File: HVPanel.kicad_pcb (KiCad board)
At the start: 2 copper layers, 7 parts, among them U1 VICOR

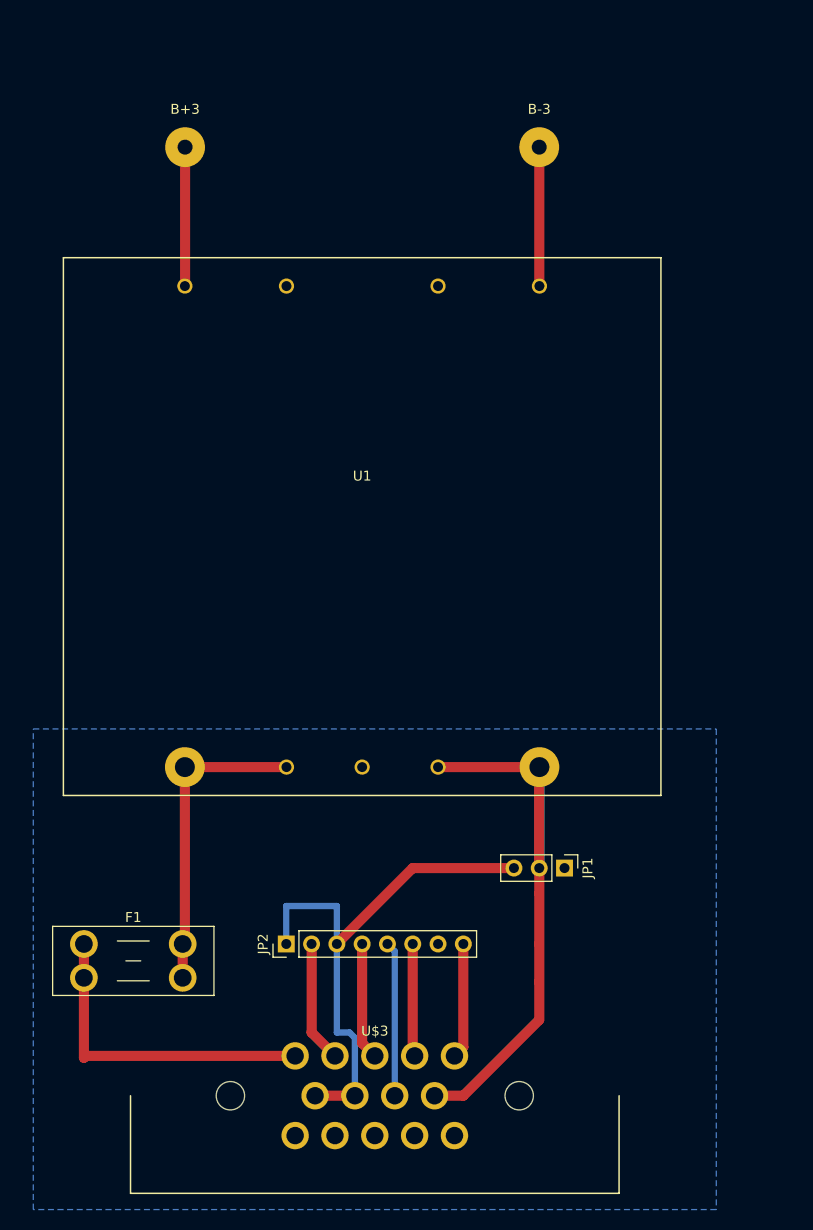
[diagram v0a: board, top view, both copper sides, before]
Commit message: Added dimensions
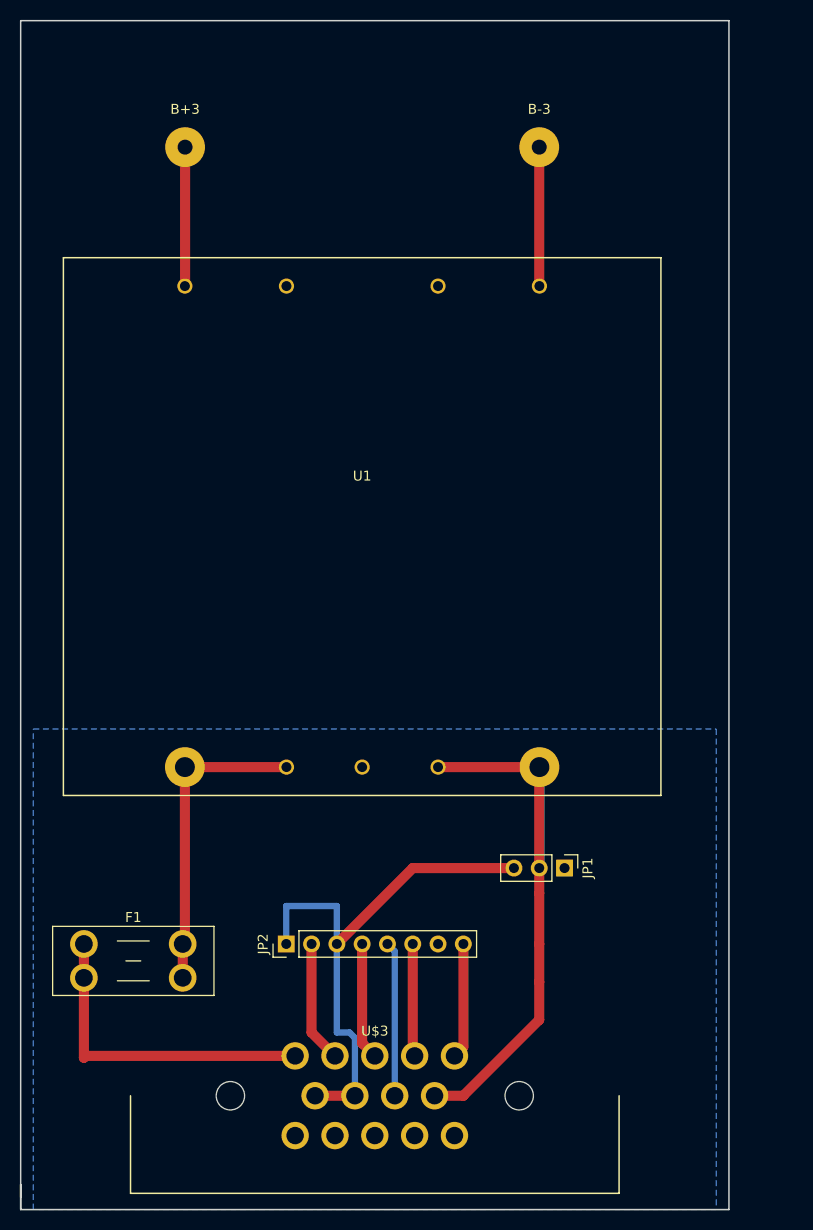
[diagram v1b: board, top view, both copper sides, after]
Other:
- board outline added: 71.1 x 119.4 mm

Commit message: added hole
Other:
- board size 71.1 x 119.4 mm -> 77.5 x 119.4 mm
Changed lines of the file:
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@@
     (links 19)
     (no_connects 0)
-    (area 67.31 46.015 135.890001 157.480001)
+    (area 57.555716 38.024999 158.344286 167.640001)
     (thickness 1.6)
-    (drawings 16)
+    (drawings 25)
     (tracks 42)
     (zones 0)
@@
     (pad "" np_thru_hole circle (at 14.5 0) (size 2.85 2.85) (drill 2.85) (layers *.Cu *.Mask))
   )
+  (dimension 3.592102 (width 0.3) (layer F.Fab)
+    (gr_text "3.592 mm" (at 141.289594 75.880405 315) (layer F.Fab)
+      (effects (font (size 1.5 1.5) (thickness 0.3)))
+    )
+    (feature1 (pts (xy 135.89 83.82) (xy 143.514189 76.195811)))
+    (feature2 (pts (xy 133.35 81.28) (xy 140.974189 73.655811)))
+    (crossbar (pts (xy 139.065 75.565) (xy 141.605 78.105)))
+    (arrow1a (pts (xy 141.605 78.105) (xy 140.393779 77.723104)))
+    (arrow1b (pts (xy 141.605 78.105) (xy 141.223104 76.893779)))
+    (arrow2a (pts (xy 139.065 75.565) (xy 139.446896 76.776221)))
+    (arrow2b (pts (xy 139.065 75.565) (xy 140.276221 75.946896)))
+  )
+  (gr_circle (center 134.62 82.55) (end 135.89 83.82) (layer Edge.Cuts) (width 0.15))
+  (dimension 3.81 (width 0.3) (layer F.Fab)
+    (gr_text "3.810 mm" (at 133.985 95.33) (layer F.Fab)
+      (effects (font (size 1.5 1.5) (thickness 0.3)))
+    )
+    (feature1 (pts (xy 135.89 81.28) (xy 135.89 96.68)))
+    (feature2 (pts (xy 132.08 81.28) (xy 132.08 96.68)))
+    (crossbar (pts (xy 132.08 93.98) (xy 135.89 93.98)))
+    (arrow1a (pts (xy 135.89 93.98) (xy 134.763496 94.566421)))
+    (arrow1b (pts (xy 135.89 93.98) (xy 134.763496 93.393579)))
+    (arrow2a (pts (xy 132.08 93.98) (xy 133.206504 94.566421)))
+    (arrow2b (pts (xy 132.08 93.98) (xy 133.206504 93.393579)))
+  )
+  (dimension 10.16 (width 0.3) (layer F.Fab)
+    (gr_text "10.160 mm" (at 138.43 86.36) (layer F.Fab)
+      (effects (font (size 1.5 1.5) (thickness 0.3)))
+    )
+    (feature1 (pts (xy 133.35 83.82) (xy 133.35 83.82)))
+    (feature2 (pts (xy 143.51 83.82) (xy 143.51 83.82)))
+    (crossbar (pts (xy 143.51 83.82) (xy 133.35 83.82)))
+    (arrow1a (pts (xy 133.35 83.82) (xy 134.476504 83.233579)))
+    (arrow1b (pts (xy 133.35 83.82) (xy 134.476504 84.406421)))
+    (arrow2a (pts (xy 143.51 83.82) (xy 142.383496 83.233579)))
+    (arrow2b (pts (xy 143.51 83.82) (xy 142.383496 84.406421)))
+  )
+  (dimension 8.89 (width 0.3) (layer F.Fab)
+    (gr_text "8.890 mm" (at 140.97 80.01) (layer F.Fab)
+      (effects (font (size 1.5 1.5) (thickness 0.3)))
+    )
+    (feature1 (pts (xy 134.62 81.28) (xy 134.62 83.98)))
+    (feature2 (pts (xy 143.51 81.28) (xy 143.51 83.98)))
+    (crossbar (pts (xy 143.51 81.28) (xy 134.62 81.28)))
+    (arrow1a (pts (xy 134.62 81.28) (xy 135.746504 80.693579)))
+    (arrow1b (pts (xy 134.62 81.28) (xy 135.746504 81.866421)))
+    (arrow2a (pts (xy 143.51 81.28) (xy 142.383496 80.693579)))
+    (arrow2b (pts (xy 143.51 81.28) (xy 142.383496 81.866421)))
+  )
+  (gr_line (start 137.16 38.1) (end 143.51 38.1) (angle 90) (layer Edge.Cuts) (width 0.15))
+  (gr_line (start 140.97 157.48) (end 143.51 157.48) (angle 90) (layer F.Fab) (width 0.2))
+  (dimension 74.93 (width 0.3) (layer F.Fab)
+    (gr_text "74.930 mm" (at 103.505 162.64) (layer F.Fab)
+      (effects (font (size 1.5 1.5) (thickness 0.3)))
+    )
+    (feature1 (pts (xy 140.97 161.29) (xy 140.97 163.99)))
+    (feature2 (pts (xy 66.04 161.29) (xy 66.04 163.99)))
+    (crossbar (pts (xy 66.04 161.29) (xy 140.97 161.29)))
+    (arrow1a (pts (xy 140.97 161.29) (xy 139.843496 161.876421)))
+    (arrow1b (pts (xy 140.97 161.29) (xy 139.843496 160.703579)))
+    (arrow2a (pts (xy 66.04 161.29) (xy 67.166504 161.876421)))
+    (arrow2b (pts (xy 66.04 161.29) (xy 67.166504 160.703579)))
+  )
+  (dimension 68.58 (width 0.3) (layer F.Fab)
+    (gr_text "68.580 mm" (at 101.6 160.02) (layer F.Fab)
+      (effects (font (size 1.5 1.5) (thickness 0.3)))
+    )
+    (feature1 (pts (xy 67.31 158.75) (xy 67.31 158.75)))
+    (feature2 (pts (xy 135.89 158.75) (xy 135.89 158.75)))
+    (crossbar (pts (xy 135.89 158.75) (xy 67.31 158.75)))
+    (arrow1a (pts (xy 67.31 158.75) (xy 68.436504 158.163579)))
+    (arrow1b (pts (xy 67.31 158.75) (xy 68.436504 159.336421)))
+    (arrow2a (pts (xy 135.89 158.75) (xy 134.763496 158.163579)))
+    (arrow2b (pts (xy 135.89 158.75) (xy 134.763496 159.336421)))
+  )
+  (gr_line (start 137.16 157.48) (end 140.97 157.48) (angle 90) (layer Edge.Cuts) (width 0.15))
+  (dimension 41.91 (width 0.3) (layer F.Fab)
+    (gr_text "41.910 mm" (at 132.08 59.69 270) (layer F.Fab)
+      (effects (font (size 1.5 1.5) (thickness 0.3)))
+    )
+    (feature1 (pts (xy 134.62 80.01) (xy 134.62 80.01)))
+    (feature2 (pts (xy 134.62 38.1) (xy 134.62 38.1)))
+    (crossbar (pts (xy 134.62 38.1) (xy 134.62 80.01)))
+    (arrow1a (pts (xy 134.62 80.01) (xy 134.033579 78.883496)))
+    (arrow1b (pts (xy 134.62 80.01) (xy 135.206421 78.883496)))
+    (arrow2a (pts (xy 134.62 38.1) (xy 134.033579 39.226504)))
+    (arrow2b (pts (xy 134.62 38.1) (xy 135.206421 39.226504)))
+  )
   (gr_line (start 66.04 154.94) (end 66.04 156.21) (angle 90) (layer Edge.Cuts) (width 0.15))
   (gr_line (start 66.04 157.48) (end 66.04 154.94) (angle 90) (layer Edge.Cuts) (width 0.15))
   (gr_line (start 66.04 38.1) (end 66.04 157.48) (angle 90) (layer Edge.Cuts) (width 0.15))
   (gr_line (start 137.16 38.1) (end 66.04 38.1) (angle 90) (layer Edge.Cuts) (width 0.15))
-  (gr_line (start 137.16 157.48) (end 137.16 38.1) (angle 90) (layer Edge.Cuts) (width 0.15))
+  (gr_line (start 143.51 157.48) (end 143.51 38.1) (angle 90) (layer Edge.Cuts) (width 0.15))
   (gr_line (start 66.04 157.48) (end 137.16 157.48) (angle 90) (layer Edge.Cuts) (width 0.15))
   (dimension 119.386755 (width 0.3) (layer F.Fab)
@@
     (arrow2b (pts (xy 144.78 167.64) (xy 144.193579 166.513496)))
   )
-  (dimension 71.12 (width 0.3) (layer F.Fab)
-    (gr_text "71.120 mm" (at 101.6 162.56) (layer F.Fab)
-      (effects (font (size 1.5 1.5) (thickness 0.3)))
-    )
-    (feature1 (pts (xy 137.16 162.56) (xy 137.16 162.56)))
-    (feature2 (pts (xy 66.04 162.56) (xy 66.04 162.56)))
-    (crossbar (pts (xy 66.04 162.56) (xy 137.16 162.56)))
-    (arrow1a (pts (xy 137.16 162.56) (xy 136.033496 163.146421)))
-    (arrow1b (pts (xy 137.16 162.56) (xy 136.033496 161.973579)))
-    (arrow2a (pts (xy 66.04 162.56) (xy 67.166504 163.146421)))
-    (arrow2b (pts (xy 66.04 162.56) (xy 67.166504 161.973579)))
-  )
   (dimension 109.22 (width 0.3) (layer F.Fab)
     (gr_text "109.220 mm" (at 64.77 101.6 270) (layer F.Fab)
@@
     (arrow2b (pts (xy 63.5 48.26) (xy 64.086421 49.386504)))
   )
-  (dimension 68.58 (width 0.3) (layer F.Fab)
-    (gr_text "68.580 mm" (at 101.6 160.02) (layer F.Fab)
-      (effects (font (size 1.5 1.5) (thickness 0.3)))
-    )
-    (feature1 (pts (xy 67.31 158.75) (xy 67.31 158.75)))
-    (feature2 (pts (xy 135.89 158.75) (xy 135.89 158.75)))
-    (crossbar (pts (xy 135.89 158.75) (xy 67.31 158.75)))
-    (arrow1a (pts (xy 67.31 158.75) (xy 68.436504 158.163579)))
-    (arrow1b (pts (xy 67.31 158.75) (xy 68.436504 159.336421)))
-    (arrow2a (pts (xy 135.89 158.75) (xy 134.763496 158.163579)))
-    (arrow2b (pts (xy 135.89 158.75) (xy 134.763496 159.336421)))
-  )
   (dimension 48.26 (width 0.3) (layer F.Fab)

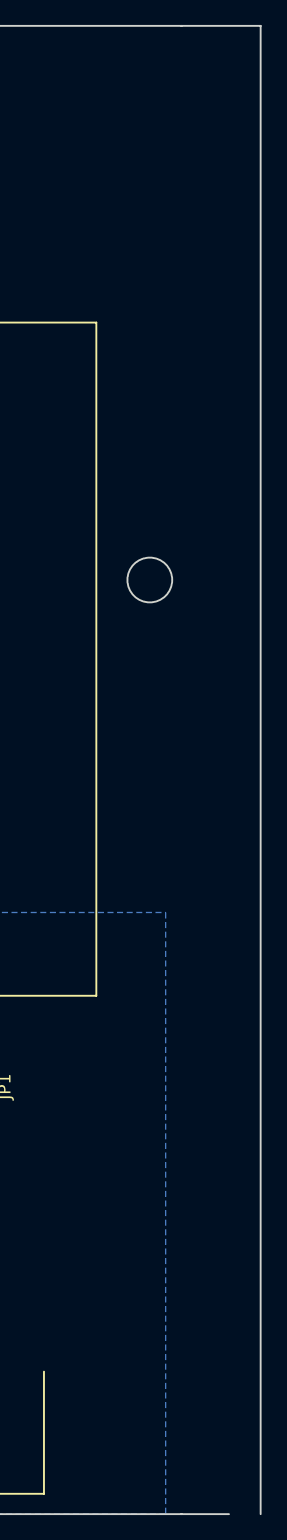
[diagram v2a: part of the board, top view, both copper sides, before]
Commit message: added 4mm hole
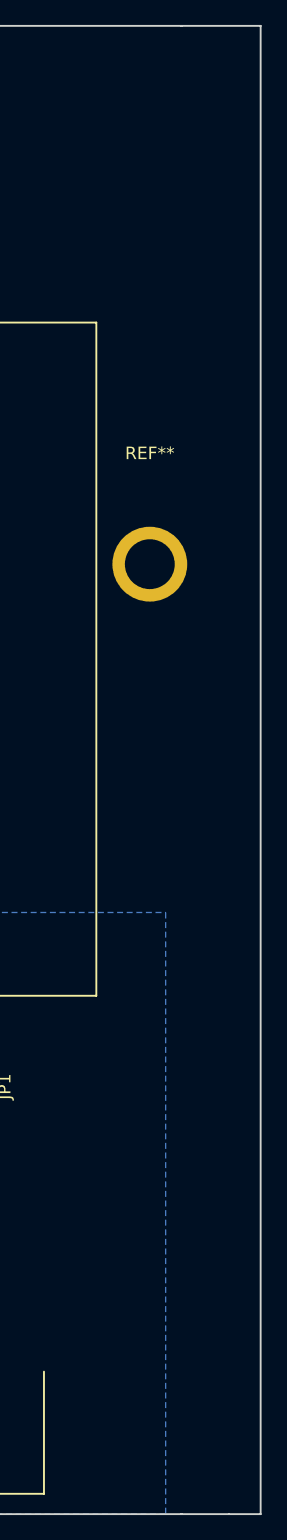
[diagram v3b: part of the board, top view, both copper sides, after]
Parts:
- added REF**: 4mmHole, TuftsRacing2018:4mmHole, F.Cu at (134.6, 81.3)
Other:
- outline, holes or cut-outs redrawn
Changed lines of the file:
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@@
     (links 19)
     (no_connects 0)
-    (area 57.555716 38.024999 158.344286 167.640001)
+    (area 65.964999 38.024999 143.585001 157.555001)
     (thickness 1.6)
-    (drawings 25)
+    (drawings 24)
     (tracks 42)
     (zones 0)
-    (modules 7)
+    (modules 8)
     (nets 22)
   )
@@
     (pad "" np_thru_hole circle (at 14.5 0) (size 2.85 2.85) (drill 2.85) (layers *.Cu *.Mask))
   )
+  (module TuftsRacing2018:4mmHole (layer F.Cu)
+    (at 134.62 81.28)
+    (fp_text reference REF** (at 0 -8.89) (layer F.SilkS)
+      (effects (font (size 1 1) (thickness 0.15)))
+    )
+    (fp_text value 4mmHole (at 0 -7.62) (layer F.Fab)
+      (effects (font (size 1 1) (thickness 0.15)))
+    )
+    (pad 1 thru_hole circle (at 0 0) (size 6 6) (drill 4) (layers *.Cu *.Mask))
+  )
+  (gr_line (start 143.51 38.1) (end 143.51 157.48) (angle 90) (layer Edge.Cuts) (width 0.15))
+  (gr_line (start 140.97 157.48) (end 143.51 157.48) (angle 90) (layer Edge.Cuts) (width 0.15))
   (dimension 3.592102 (width 0.3) (layer F.Fab)
     (gr_text "3.592 mm" (at 141.289594 75.880405 315) (layer F.Fab)
@@
     (arrow2b (pts (xy 139.065 75.565) (xy 140.276221 75.946896)))
   )
-  (gr_circle (center 134.62 82.55) (end 135.89 83.82) (layer Edge.Cuts) (width 0.15))
   (dimension 3.81 (width 0.3) (layer F.Fab)
     (gr_text "3.810 mm" (at 133.985 95.33) (layer F.Fab)
@@
   )
   (gr_line (start 137.16 38.1) (end 143.51 38.1) (angle 90) (layer Edge.Cuts) (width 0.15))
-  (gr_line (start 140.97 157.48) (end 143.51 157.48) (angle 90) (layer F.Fab) (width 0.2))
   (dimension 74.93 (width 0.3) (layer F.Fab)
     (gr_text "74.930 mm" (at 103.505 162.64) (layer F.Fab)
@@
   (gr_line (start 66.04 38.1) (end 66.04 157.48) (angle 90) (layer Edge.Cuts) (width 0.15))
   (gr_line (start 137.16 38.1) (end 66.04 38.1) (angle 90) (layer Edge.Cuts) (width 0.15))
-  (gr_line (start 143.51 157.48) (end 143.51 38.1) (angle 90) (layer Edge.Cuts) (width 0.15))
   (gr_line (start 66.04 157.48) (end 137.16 157.48) (angle 90) (layer Edge.Cuts) (width 0.15))
   (dimension 119.386755 (width 0.3) (layer F.Fab)
